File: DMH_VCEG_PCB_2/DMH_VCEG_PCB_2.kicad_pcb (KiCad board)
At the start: 2 copper layers, 96 x 175 mm, 0 parts

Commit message: Copied PCB 1 as PCB 2
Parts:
- added C1: 100pF, Capacitor_THT:C_Disc_D3.8mm_W2.6mm_P2.50mm, F.Cu at (285.9, 177.0)
- added C12: 100pF, Capacitor_THT:C_Disc_D3.8mm_W2.6mm_P2.50mm, F.Cu at (286.2, 86.7)
- added C13: 100pF, Capacitor_THT:C_Disc_D3.8mm_W2.6mm_P2.50mm, F.Cu at (286.2, 90.1)
- added C14: 100pF, Capacitor_THT:C_Disc_D3.8mm_W2.6mm_P2.50mm, F.Cu at (286.2, 93.6)
- added C15: 10nF, Capacitor_THT:C_Disc_D4.3mm_W1.9mm_P5.00mm, F.Cu at (286.2, 97.0)
- added C16: 1nF, Capacitor_THT:C_Disc_D4.3mm_W1.9mm_P5.00mm, F.Cu at (286.2, 100.5)
- added C17: 1nF, Capacitor_THT:C_Disc_D4.3mm_W1.9mm_P5.00mm, F.Cu at (286.2, 103.9)
- added C18: 1uF, Capacitor_THT:C_Disc_D4.3mm_W1.9mm_P5.00mm, F.Cu at (286.2, 107.4)
- added C19: 10uF, Capacitor_THT:CP_Radial_D5.0mm_P2.00mm, F.Cu at (242.5, 136.8)
- added C2: 100pF, Capacitor_THT:C_Disc_D3.8mm_W2.6mm_P2.50mm, F.Cu at (285.9, 180.4)
- added C20: 100nF, Capacitor_THT:C_Disc_D4.3mm_W1.9mm_P5.00mm, F.Cu at (286.2, 110.8)
- added C23: 47uF, Capacitor_THT:CP_Radial_D5.0mm_P2.00mm, B.Cu at (75.5, 46.7)
- added C24: 47uF, Capacitor_THT:CP_Radial_D5.0mm_P2.00mm, B.Cu at (124.5, 44.8)
- added C25: 100nF, Capacitor_THT:C_Disc_D4.3mm_W1.9mm_P5.00mm, F.Cu at (296.1, 157.5)
- added C26: 100nF, Capacitor_THT:C_Disc_D4.3mm_W1.9mm_P5.00mm, F.Cu at (296.1, 160.9)
- added C27: 100nF, Capacitor_THT:C_Disc_D4.3mm_W1.9mm_P5.00mm, F.Cu at (296.1, 164.4)
- added C28: 100nF, Capacitor_THT:C_Disc_D4.3mm_W1.9mm_P5.00mm, F.Cu at (296.1, 167.8)
- added C29: 100nF, Capacitor_THT:C_Disc_D4.3mm_W1.9mm_P5.00mm, F.Cu at (296.1, 171.3)
- added C3: 100pF, Capacitor_THT:C_Disc_D3.8mm_W2.6mm_P2.50mm, F.Cu at (285.9, 183.9)
- added C30: 100nF, Capacitor_THT:C_Disc_D4.3mm_W1.9mm_P5.00mm, F.Cu at (296.1, 174.7)
- added C31: 100nF, Capacitor_THT:C_Disc_D4.3mm_W1.9mm_P5.00mm, F.Cu at (296.1, 178.2)
- added C32: 100nF, Capacitor_THT:C_Disc_D4.3mm_W1.9mm_P5.00mm, F.Cu at (296.1, 181.6)
- added C33: 100nF, Capacitor_THT:C_Disc_D4.3mm_W1.9mm_P5.00mm, F.Cu at (296.1, 185.1)
- added C34: 100nF, Capacitor_THT:C_Disc_D4.3mm_W1.9mm_P5.00mm, F.Cu at (296.1, 188.5)
- added C35: 100nF, Capacitor_THT:C_Disc_D4.3mm_W1.9mm_P5.00mm, F.Cu at (304.2, 157.5)
- added C4: 10nF, Capacitor_THT:C_Disc_D4.3mm_W1.9mm_P5.00mm, F.Cu at (285.9, 187.3)
- added C40: 100nF, Capacitor_THT:C_Disc_D4.3mm_W1.9mm_P5.00mm, F.Cu at (304.2, 174.7)
- added C41: 100nF, Capacitor_THT:C_Disc_D4.3mm_W1.9mm_P5.00mm, F.Cu at (304.2, 178.2)
- added C42: 100nF, Capacitor_THT:C_Disc_D4.3mm_W1.9mm_P5.00mm, F.Cu at (304.2, 181.6)
- added C43: 100nF, Capacitor_THT:C_Disc_D4.3mm_W1.9mm_P5.00mm, F.Cu at (304.2, 185.1)
- added C44: 100nF, Capacitor_THT:C_Disc_D4.3mm_W1.9mm_P5.00mm, F.Cu at (304.2, 188.5)
- added C45: 100nF, Capacitor_THT:C_Disc_D4.3mm_W1.9mm_P5.00mm, F.Cu at (312.4, 157.5)
- added C46: 100nF, Capacitor_THT:C_Disc_D4.3mm_W1.9mm_P5.00mm, F.Cu at (312.4, 160.9)
- added C47: 100nF, Capacitor_THT:C_Disc_D4.3mm_W1.9mm_P5.00mm, F.Cu at (312.4, 164.4)
- added C48: 100nF, Capacitor_THT:C_Disc_D4.3mm_W1.9mm_P5.00mm, F.Cu at (312.4, 167.8)
- added C49: 100nF, Capacitor_THT:C_Disc_D4.3mm_W1.9mm_P5.00mm, F.Cu at (312.4, 171.3)
- added C5: 1nF, Capacitor_THT:C_Disc_D4.3mm_W1.9mm_P5.00mm, F.Cu at (285.9, 190.8)
- added C50: 100nF, Capacitor_THT:C_Disc_D4.3mm_W1.9mm_P5.00mm, F.Cu at (312.4, 174.7)
- added C6: 1nF, Capacitor_THT:C_Disc_D4.3mm_W1.9mm_P5.00mm, F.Cu at (285.9, 194.2)
- added C7: 1uF, Capacitor_THT:C_Disc_D4.3mm_W1.9mm_P5.00mm, F.Cu at (285.9, 197.7)
- added C8: 10uF, Capacitor_THT:CP_Radial_D5.0mm_P2.00mm, F.Cu at (242.2, 227.1)
- added C9: 100nF, Capacitor_THT:C_Disc_D4.3mm_W1.9mm_P5.00mm, F.Cu at (285.9, 201.1)
- added D1: SB140-, Diode_THT:D_DO-41_SOD81_P10.16mm_Horizontal, B.Cu at (117.8, 44.2)
- added D15: 1N4148, Diode_THT:D_DO-35_SOD27_P7.62mm_Horizontal, F.Cu at (282.2, 114.5)
- added D16: 1N4148, Diode_THT:D_DO-35_SOD27_P7.62mm_Horizontal, F.Cu at (282.2, 118.0)
- added D17: 1N4148, Diode_THT:D_DO-35_SOD27_P7.62mm_Horizontal, F.Cu at (282.2, 121.5)
- added D18: 1N4148, Diode_THT:D_DO-35_SOD27_P7.62mm_Horizontal, F.Cu at (282.2, 125.1)
- added D19: 1N4148, Diode_THT:D_DO-35_SOD27_P7.62mm_Horizontal, F.Cu at (282.2, 128.7)
- added D2: SB140+, Diode_THT:D_DO-41_SOD81_P10.16mm_Horizontal, B.Cu at (82.2, 54.3)
- added D20: ZPD10, Diode_THT:D_DO-35_SOD27_P7.62mm_Horizontal, F.Cu at (228.4, 135.3)
- added D3: 1N4148, Diode_THT:D_DO-35_SOD27_P7.62mm_Horizontal, F.Cu at (281.9, 204.7)
- added D4: 1N4148, Diode_THT:D_DO-35_SOD27_P7.62mm_Horizontal, F.Cu at (281.9, 208.3)
- added D5: 1N4148, Diode_THT:D_DO-35_SOD27_P7.62mm_Horizontal, F.Cu at (281.9, 211.8)
- added D6: 1N4148, Diode_THT:D_DO-35_SOD27_P7.62mm_Horizontal, F.Cu at (281.9, 215.4)
- added D7: 1N4148, Diode_THT:D_DO-35_SOD27_P7.62mm_Horizontal, F.Cu at (281.9, 218.9)
- added D8: ZPD10, Diode_THT:D_DO-35_SOD27_P7.62mm_Horizontal, F.Cu at (228.1, 225.6)
- added J1: TS_Jack_6.35mm_Sw, SynthStuff:CUI_MJ-63052A, F.Cu at (33.5, 190.2)
- added J10: TS_Jack_6.35mm_Sw, SynthStuff:CUI_MJ-63052A, F.Cu at (33.5, 208.8)
- added J100: IDC_02x08, SynthStuff:IDC-Header_2x08_P2.54mm_Vertical_Eurorack, B.Cu at (108.9, 48.8)
- added J11: TS_Jack_6.35mm_Sw, SynthStuff:CUI_MJ-63052A, F.Cu at (166.5, 190.2)
- added J12: TS_Jack_6.35mm_Sw, SynthStuff:CUI_MJ-63052A, F.Cu at (150.0, 190.2)
- added J13: TS_Jack_6.35mm_Sw, SynthStuff:CUI_MJ-63052A, F.Cu at (133.5, 190.2)
- added J14: TS_Jack_6.35mm_Sw, SynthStuff:CUI_MJ-63052A, F.Cu at (117.0, 190.2)
- added J15: TS_Jack_6.35mm_Sw, SynthStuff:CUI_MJ-63052A, F.Cu at (117.0, 208.8)
- added J16: TS_Jack_6.35mm_Sw, SynthStuff:CUI_MJ-63052A, F.Cu at (166.5, 171.8)
- added J17: TS_Jack_6.35mm_Sw, SynthStuff:CUI_MJ-63052A, F.Cu at (100.0, 208.8)
- added J18: TS_Jack_6.35mm_Sw, SynthStuff:CUI_MJ-63052A, F.Cu at (133.5, 208.8)
- added J19: TS_Jack_6.35mm_Sw, SynthStuff:CUI_MJ-63052A, F.Cu at (150.0, 208.8)
- added J2: TS_Jack_6.35mm_Sw, SynthStuff:CUI_MJ-63052A, F.Cu at (50.0, 190.2)
- added J20: TS_Jack_6.35mm_Sw, SynthStuff:CUI_MJ-63052A, F.Cu at (166.5, 208.8)
- added J200: IDC_02x08, SynthStuff:IDC-Header_2x08_P2.54mm_Vertical_BackBone, B.Cu at (91.1, 175.5)
- added J21: Conn_01x10_PinHeader, Connector_PinHeader_2.54mm:PinHeader_1x10_P2.54mm_Vertical, F.Cu at (317.1, 109.0)
- added J22: Conn_01x10_PinHeader, Connector_PinHeader_2.54mm:PinHeader_1x10_P2.54mm_Vertical, F.Cu at (321.7, 109.0)
- added J23: Conn_01x10_PinHeader, Connector_PinHeader_2.54mm:PinHeader_1x10_P2.54mm_Vertical, F.Cu at (326.2, 109.0)
- added J24: Conn_01x10_PinHeader, Connector_PinHeader_2.54mm:PinHeader_1x10_P2.54mm_Vertical, F.Cu at (301.3, 109.0)
- added J25: Conn_01x10_PinHeader, Connector_PinHeader_2.54mm:PinHeader_1x10_P2.54mm_Vertical, F.Cu at (305.9, 109.0)
- added J26: Conn_01x10_PinHeader, Connector_PinHeader_2.54mm:PinHeader_1x10_P2.54mm_Vertical, F.Cu at (310.5, 109.0)
- added J27: Conn_01x06_PinHeader, Connector_PinHeader_2.54mm:PinHeader_1x06_P2.54mm_Vertical, F.Cu at (330.8, 109.0)
- added J3: TS_Jack_6.35mm_Sw, SynthStuff:CUI_MJ-63052A, F.Cu at (66.5, 190.2)
- added J4: TS_Jack_6.35mm_Sw, SynthStuff:CUI_MJ-63052A, F.Cu at (83.0, 190.2)
- added J5: TS_Jack_6.35mm_Sw, SynthStuff:CUI_MJ-63052A, F.Cu at (83.0, 208.8)
- added J6: TS_Jack_6.35mm_Sw, SynthStuff:CUI_MJ-63052A, F.Cu at (33.5, 171.8)
- added J7: TS_Jack_6.35mm_Sw, SynthStuff:CUI_MJ-63052A, F.Cu at (100.0, 190.2)
- added J8: TS_Jack_6.35mm_Sw, SynthStuff:CUI_MJ-63052A, F.Cu at (66.5, 208.8)
- added J9: TS_Jack_6.35mm_Sw, SynthStuff:CUI_MJ-63052A, F.Cu at (50.0, 208.8)
- added Q1: BC548, Package_TO_SOT_THT:TO-92L_Inline_Wide, F.Cu at (228.0, 230.7)
- added Q2: BC558, Package_TO_SOT_THT:TO-92L_Inline_Wide, F.Cu at (241.8, 233.6)
- added Q3: BC548, Package_TO_SOT_THT:TO-92L_Inline_Wide, F.Cu at (228.0, 236.3)
- added Q5: BC548, Package_TO_SOT_THT:TO-92L_Inline_Wide, F.Cu at (228.3, 140.4)
- added Q6: BC558, Package_TO_SOT_THT:TO-92L_Inline_Wide, F.Cu at (242.1, 143.3)
- added Q7: BC548, Package_TO_SOT_THT:TO-92L_Inline_Wide, F.Cu at (228.3, 146.0)
- added R1: 100k, Resistor_THT:R_Axial_DIN0207_L6.3mm_D2.5mm_P7.62mm_Horizontal, F.Cu at (228.1, 177.3)
- added R10: 10k, Resistor_THT:R_Axial_DIN0207_L6.3mm_D2.5mm_P7.62mm_Horizontal, F.Cu at (228.1, 213.7)
- added R100: 330k, Resistor_THT:R_Axial_DIN0207_L6.3mm_D2.5mm_P7.62mm_Horizontal, F.Cu at (239.1, 119.4)
- added R101: 100k, Resistor_THT:R_Axial_DIN0207_L6.3mm_D2.5mm_P7.62mm_Horizontal, F.Cu at (239.1, 123.4)
- added R102: 680R, Resistor_THT:R_Axial_DIN0207_L6.3mm_D2.5mm_P7.62mm_Horizontal, F.Cu at (239.1, 127.5)
- added R103: 100k, Resistor_THT:R_Axial_DIN0207_L6.3mm_D2.5mm_P7.62mm_Horizontal, F.Cu at (239.1, 131.5)
- added R104: 100k, Resistor_THT:R_Axial_DIN0207_L6.3mm_D2.5mm_P7.62mm_Horizontal, F.Cu at (249.9, 87.0)
- added R105: 100k, Resistor_THT:R_Axial_DIN0207_L6.3mm_D2.5mm_P7.62mm_Horizontal, F.Cu at (249.9, 91.0)
- added R106: 470R, Resistor_THT:R_Axial_DIN0207_L6.3mm_D2.5mm_P7.62mm_Horizontal, F.Cu at (249.9, 95.1)
- added R107: 100k, Resistor_THT:R_Axial_DIN0207_L6.3mm_D2.5mm_P7.62mm_Horizontal, F.Cu at (249.9, 99.1)
- added R108: 125k, Resistor_THT:R_Axial_DIN0207_L6.3mm_D2.5mm_P7.62mm_Horizontal, F.Cu at (249.9, 103.2)
- added R109: 100k, Resistor_THT:R_Axial_DIN0207_L6.3mm_D2.5mm_P7.62mm_Horizontal, F.Cu at (249.9, 107.2)
- added R11: 10k, Resistor_THT:R_Axial_DIN0207_L6.3mm_D2.5mm_P7.62mm_Horizontal, F.Cu at (228.1, 217.8)
- added R110: 470R, Resistor_THT:R_Axial_DIN0207_L6.3mm_D2.5mm_P7.62mm_Horizontal, F.Cu at (249.9, 111.3)
- added R111: 100k, Resistor_THT:R_Axial_DIN0207_L6.3mm_D2.5mm_P7.62mm_Horizontal, F.Cu at (249.9, 115.3)
- added R112: 100k, Resistor_THT:R_Axial_DIN0207_L6.3mm_D2.5mm_P7.62mm_Horizontal, F.Cu at (249.9, 119.4)
- added R113: 10k, Resistor_THT:R_Axial_DIN0207_L6.3mm_D2.5mm_P7.62mm_Horizontal, F.Cu at (249.9, 123.4)
- added R114: 1k, Resistor_THT:R_Axial_DIN0207_L6.3mm_D2.5mm_P7.62mm_Horizontal, F.Cu at (249.9, 127.5)
- added R115: 10k, Resistor_THT:R_Axial_DIN0207_L6.3mm_D2.5mm_P7.62mm_Horizontal, F.Cu at (249.9, 131.5)
- added R116: 470k, Resistor_THT:R_Axial_DIN0207_L6.3mm_D2.5mm_P7.62mm_Horizontal, F.Cu at (260.7, 87.0)
- added R117: 10k, Resistor_THT:R_Axial_DIN0207_L6.3mm_D2.5mm_P7.62mm_Horizontal, F.Cu at (260.7, 91.0)
- added R118: 470k, Resistor_THT:R_Axial_DIN0207_L6.3mm_D2.5mm_P7.62mm_Horizontal, F.Cu at (260.7, 95.1)
- added R119: 330k, Resistor_THT:R_Axial_DIN0207_L6.3mm_D2.5mm_P7.62mm_Horizontal, F.Cu at (260.7, 99.1)
- added R12: 10k, Resistor_THT:R_Axial_DIN0207_L6.3mm_D2.5mm_P7.62mm_Horizontal, F.Cu at (228.1, 221.8)
- added R120: 10k, Resistor_THT:R_Axial_DIN0207_L6.3mm_D2.5mm_P7.62mm_Horizontal, F.Cu at (260.7, 103.2)
- added R121: 300k, Resistor_THT:R_Axial_DIN0207_L6.3mm_D2.5mm_P7.62mm_Horizontal, F.Cu at (260.7, 107.2)
- added R122: 330k, Resistor_THT:R_Axial_DIN0207_L6.3mm_D2.5mm_P7.62mm_Horizontal, F.Cu at (260.7, 111.3)
- added R123: 10k, Resistor_THT:R_Axial_DIN0207_L6.3mm_D2.5mm_P7.62mm_Horizontal, F.Cu at (260.7, 115.3)
- added R13: 470k, Resistor_THT:R_Axial_DIN0207_L6.3mm_D2.5mm_P7.62mm_Horizontal, F.Cu at (238.8, 177.3)
- added R14: 10k, Resistor_THT:R_Axial_DIN0207_L6.3mm_D2.5mm_P7.62mm_Horizontal, F.Cu at (238.8, 181.3)
- added R15: 100k, Resistor_THT:R_Axial_DIN0207_L6.3mm_D2.5mm_P7.62mm_Horizontal, F.Cu at (238.8, 185.4)
- added R16: 10k, Resistor_THT:R_Axial_DIN0207_L6.3mm_D2.5mm_P7.62mm_Horizontal, F.Cu at (238.8, 189.4)
- added R17: 10k, Resistor_THT:R_Axial_DIN0207_L6.3mm_D2.5mm_P7.62mm_Horizontal, F.Cu at (238.8, 193.5)
- added R18: 10k, Resistor_THT:R_Axial_DIN0207_L6.3mm_D2.5mm_P7.62mm_Horizontal, F.Cu at (238.8, 197.5)
- added R19: 100k, Resistor_THT:R_Axial_DIN0207_L6.3mm_D2.5mm_P7.62mm_Horizontal, F.Cu at (238.8, 201.6)
- added R2: 100k, Resistor_THT:R_Axial_DIN0207_L6.3mm_D2.5mm_P7.62mm_Horizontal, F.Cu at (228.1, 181.3)
- added R20: 300k, Resistor_THT:R_Axial_DIN0207_L6.3mm_D2.5mm_P7.62mm_Horizontal, F.Cu at (238.8, 205.6)
- added R21: 330k, Resistor_THT:R_Axial_DIN0207_L6.3mm_D2.5mm_P7.62mm_Horizontal, F.Cu at (238.8, 209.7)
- added R22: 100k, Resistor_THT:R_Axial_DIN0207_L6.3mm_D2.5mm_P7.62mm_Horizontal, F.Cu at (238.8, 213.7)
- added R23: 680R, Resistor_THT:R_Axial_DIN0207_L6.3mm_D2.5mm_P7.62mm_Horizontal, F.Cu at (238.8, 217.8)
- added R24: 100k, Resistor_THT:R_Axial_DIN0207_L6.3mm_D2.5mm_P7.62mm_Horizontal, F.Cu at (238.8, 221.8)
- added R25: 100k, Resistor_THT:R_Axial_DIN0207_L6.3mm_D2.5mm_P7.62mm_Horizontal, F.Cu at (249.6, 177.3)
- added R26: 100k, Resistor_THT:R_Axial_DIN0207_L6.3mm_D2.5mm_P7.62mm_Horizontal, F.Cu at (249.6, 181.3)
- added R27: 470R, Resistor_THT:R_Axial_DIN0207_L6.3mm_D2.5mm_P7.62mm_Horizontal, F.Cu at (249.6, 185.4)
- added R28: 100k, Resistor_THT:R_Axial_DIN0207_L6.3mm_D2.5mm_P7.62mm_Horizontal, F.Cu at (249.6, 189.4)
- added R29: 125k, Resistor_THT:R_Axial_DIN0207_L6.3mm_D2.5mm_P7.62mm_Horizontal, F.Cu at (249.6, 193.5)
- added R3: 22k, Resistor_THT:R_Axial_DIN0207_L6.3mm_D2.5mm_P7.62mm_Horizontal, F.Cu at (228.1, 185.4)
- added R30: 100k, Resistor_THT:R_Axial_DIN0207_L6.3mm_D2.5mm_P7.62mm_Horizontal, F.Cu at (249.6, 197.5)
- added R31: 470R, Resistor_THT:R_Axial_DIN0207_L6.3mm_D2.5mm_P7.62mm_Horizontal, F.Cu at (249.6, 201.6)
- added R32: 100k, Resistor_THT:R_Axial_DIN0207_L6.3mm_D2.5mm_P7.62mm_Horizontal, F.Cu at (249.6, 205.6)
- added R33: 100k, Resistor_THT:R_Axial_DIN0207_L6.3mm_D2.5mm_P7.62mm_Horizontal, F.Cu at (249.6, 209.7)
- added R34: 10k, Resistor_THT:R_Axial_DIN0207_L6.3mm_D2.5mm_P7.62mm_Horizontal, F.Cu at (249.6, 213.7)
- added R35: 1k, Resistor_THT:R_Axial_DIN0207_L6.3mm_D2.5mm_P7.62mm_Horizontal, F.Cu at (249.6, 217.8)
- added R36: 10k, Resistor_THT:R_Axial_DIN0207_L6.3mm_D2.5mm_P7.62mm_Horizontal, F.Cu at (249.6, 221.8)
- added R37: 470k, Resistor_THT:R_Axial_DIN0207_L6.3mm_D2.5mm_P7.62mm_Horizontal, F.Cu at (260.4, 177.3)
- added R38: 10k, Resistor_THT:R_Axial_DIN0207_L6.3mm_D2.5mm_P7.62mm_Horizontal, F.Cu at (260.4, 181.3)
- added R39: 470k, Resistor_THT:R_Axial_DIN0207_L6.3mm_D2.5mm_P7.62mm_Horizontal, F.Cu at (260.4, 185.4)
- added R4: 100k, Resistor_THT:R_Axial_DIN0207_L6.3mm_D2.5mm_P7.62mm_Horizontal, F.Cu at (228.1, 189.4)
- added R40: 330k, Resistor_THT:R_Axial_DIN0207_L6.3mm_D2.5mm_P7.62mm_Horizontal, F.Cu at (260.4, 189.4)
- added R41: 10k, Resistor_THT:R_Axial_DIN0207_L6.3mm_D2.5mm_P7.62mm_Horizontal, F.Cu at (260.4, 193.5)
- added R42: 300k, Resistor_THT:R_Axial_DIN0207_L6.3mm_D2.5mm_P7.62mm_Horizontal, F.Cu at (260.4, 197.5)
- added R43: 330k, Resistor_THT:R_Axial_DIN0207_L6.3mm_D2.5mm_P7.62mm_Horizontal, F.Cu at (260.4, 201.6)
- added R44: 10k, Resistor_THT:R_Axial_DIN0207_L6.3mm_D2.5mm_P7.62mm_Horizontal, F.Cu at (260.4, 205.6)
- added R5: 22k, Resistor_THT:R_Axial_DIN0207_L6.3mm_D2.5mm_P7.62mm_Horizontal, F.Cu at (228.1, 193.5)
- added R6: 1M, Resistor_THT:R_Axial_DIN0207_L6.3mm_D2.5mm_P7.62mm_Horizontal, F.Cu at (228.1, 197.5)
- added R7: 1M, Resistor_THT:R_Axial_DIN0207_L6.3mm_D2.5mm_P7.62mm_Horizontal, F.Cu at (228.1, 201.6)
- added R8: 22k, Resistor_THT:R_Axial_DIN0207_L6.3mm_D2.5mm_P7.62mm_Horizontal, F.Cu at (228.1, 205.6)
- added R80: 100k, Resistor_THT:R_Axial_DIN0207_L6.3mm_D2.5mm_P7.62mm_Horizontal, F.Cu at (228.4, 87.0)
- added R81: 100k, Resistor_THT:R_Axial_DIN0207_L6.3mm_D2.5mm_P7.62mm_Horizontal, F.Cu at (228.4, 91.0)
- added R82: 22k, Resistor_THT:R_Axial_DIN0207_L6.3mm_D2.5mm_P7.62mm_Horizontal, F.Cu at (228.4, 95.1)
- added R83: 100k, Resistor_THT:R_Axial_DIN0207_L6.3mm_D2.5mm_P7.62mm_Horizontal, F.Cu at (228.4, 99.1)
- added R84: 22k, Resistor_THT:R_Axial_DIN0207_L6.3mm_D2.5mm_P7.62mm_Horizontal, F.Cu at (228.4, 103.2)
- added R85: 1M, Resistor_THT:R_Axial_DIN0207_L6.3mm_D2.5mm_P7.62mm_Horizontal, F.Cu at (228.4, 107.2)
- added R86: 1M, Resistor_THT:R_Axial_DIN0207_L6.3mm_D2.5mm_P7.62mm_Horizontal, F.Cu at (228.4, 111.3)
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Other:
- board size 96 x 175 mm -> 148 x 175 mm

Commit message: Placed front panel components on PCB 2
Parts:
- removed C1, C12, C13, C14, C2, C3: 100pF, Capacitor_THT:C_Disc_D3.8mm_W2.6mm_P2.50mm
- removed C15, C4: 10nF, Capacitor_THT:C_Disc_D4.3mm_W1.9mm_P5.00mm
- removed C16, C17, C5, C6: 1nF, Capacitor_THT:C_Disc_D4.3mm_W1.9mm_P5.00mm
- removed C18, C7: 1uF, Capacitor_THT:C_Disc_D4.3mm_W1.9mm_P5.00mm
- removed C19, C8: 10uF, Capacitor_THT:CP_Radial_D5.0mm_P2.00mm
- removed C20, C25, C26, C27, C28, C29, C30, C31, C32, C33, C34, C35, C40, C41, C42, C43, C44, C45, C46, C47, C48, C49, C50, C9: 100nF, Capacitor_THT:C_Disc_D4.3mm_W1.9mm_P5.00mm
- removed C23, C24: 47uF, Capacitor_THT:CP_Radial_D5.0mm_P2.00mm
- removed D1: SB140-, Diode_THT:D_DO-41_SOD81_P10.16mm_Horizontal
- removed D15, D16, D17, D18, D19, D3, D4, D5, D6, D7: 1N4148, Diode_THT:D_DO-35_SOD27_P7.62mm_Horizontal
- removed D2: SB140+, Diode_THT:D_DO-41_SOD81_P10.16mm_Horizontal
- removed D20, D8: ZPD10, Diode_THT:D_DO-35_SOD27_P7.62mm_Horizontal
- removed J1, J10, J11, J12, J13, J14, J15, J16, J17, J18, J19, J2, J20, J3, J4, J5, J6, J7, J8, J9: TS_Jack_6.35mm_Sw, SynthStuff:CUI_MJ-63052A
- removed J100: IDC_02x08, SynthStuff:IDC-Header_2x08_P2.54mm_Vertical_Eurorack
- removed J200: IDC_02x08, SynthStuff:IDC-Header_2x08_P2.54mm_Vertical_BackBone
- removed Q1, Q3, Q5, Q7: BC548, Package_TO_SOT_THT:TO-92L_Inline_Wide
- removed Q2, Q6: BC558, Package_TO_SOT_THT:TO-92L_Inline_Wide
- removed R1, R101, R103, R104, R105, R107, R109, R111, R112, R15, R19, R2, R22, R24, R25, R26, R28, R30, R32, R33, R4, R80, R81, R83, R94, R98: 100k, Resistor_THT:R_Axial_DIN0207_L6.3mm_D2.5mm_P7.62mm_Horizontal
- removed R10, R11, R113, R115, R117, R12, R120, R123, R14, R16, R17, R18, R34, R36, R38, R41, R44, R89, R90, R91, R93, R95, R96, R97: 10k, Resistor_THT:R_Axial_DIN0207_L6.3mm_D2.5mm_P7.62mm_Horizontal
- removed R100, R119, R122, R21, R40, R43: 330k, Resistor_THT:R_Axial_DIN0207_L6.3mm_D2.5mm_P7.62mm_Horizontal
- removed R102, R23: 680R, Resistor_THT:R_Axial_DIN0207_L6.3mm_D2.5mm_P7.62mm_Horizontal
- removed R106, R110, R27, R31, R88, R9: 470R, Resistor_THT:R_Axial_DIN0207_L6.3mm_D2.5mm_P7.62mm_Horizontal
- removed R108, R29: 125k, Resistor_THT:R_Axial_DIN0207_L6.3mm_D2.5mm_P7.62mm_Horizontal
- removed R114, R35: 1k, Resistor_THT:R_Axial_DIN0207_L6.3mm_D2.5mm_P7.62mm_Horizontal
- removed R116, R118, R13, R37, R39, R92: 470k, Resistor_THT:R_Axial_DIN0207_L6.3mm_D2.5mm_P7.62mm_Horizontal
- removed R121, R20, R42, R99: 300k, Resistor_THT:R_Axial_DIN0207_L6.3mm_D2.5mm_P7.62mm_Horizontal
- removed R3, R5, R8, R82, R84, R87: 22k, Resistor_THT:R_Axial_DIN0207_L6.3mm_D2.5mm_P7.62mm_Horizontal
- removed R6, R7, R85, R86: 1M, Resistor_THT:R_Axial_DIN0207_L6.3mm_D2.5mm_P7.62mm_Horizontal
- removed RV1, RV12, RV2, RV31, RV32, RV36, RV37, RV38, RV42, RV6, RV7, RV8: 50k, Potentiometer_THT:Potentiometer_Bourns_3296W_Vertical
- removed RV11, RV41: 10k, Potentiometer_THT:Potentiometer_Bourns_3296W_Vertical
- removed RV13, RV3, RV33, RV39, RV43, RV9: 100k, Potentiometer_THT:Potentiometer_Bourns_3296W_Vertical
- removed U11, U2: 4001, Package_DIP:DIP-14_W7.62mm_Socket
- removed U12, U3: 40106, Package_DIP:DIP-14_W7.62mm_Socket
- removed U13, U4: CD4066BE, Package_DIP:DIP-14_W7.62mm
- removed U14, U15, U16, U5, U6, U7: TL074, Package_DIP:DIP-14_W7.62mm_Socket
- added C10: 1uF, Capacitor_THT:C_Disc_D4.3mm_W1.9mm_P5.00mm, F.Cu at (214.2, 123.2)
- added C11: 10uF, Capacitor_THT:CP_Radial_D5.0mm_P2.00mm, F.Cu at (231.3, 124.8)
- added C21: 1uF, Capacitor_THT:C_Disc_D4.3mm_W1.9mm_P5.00mm, F.Cu at (261.0, 155.1)
- added C22: 10uF, Capacitor_THT:CP_Radial_D5.0mm_P2.00mm, F.Cu at (223.1, 173.6)
- added C36: 100nF, Capacitor_THT:C_Disc_D4.3mm_W1.9mm_P5.00mm, F.Cu at (333.2, 86.8)
- added C37: 100nF, Capacitor_THT:C_Disc_D4.3mm_W1.9mm_P5.00mm, F.Cu at (333.2, 90.2)
- added C38: 100nF, Capacitor_THT:C_Disc_D4.3mm_W1.9mm_P5.00mm, F.Cu at (333.2, 93.7)
- added C39: 100nF, Capacitor_THT:C_Disc_D4.3mm_W1.9mm_P5.00mm, F.Cu at (333.2, 97.2)
- added C51: 100nF, Capacitor_THT:C_Disc_D4.3mm_W1.9mm_P5.00mm, F.Cu at (333.2, 100.6)
- added C52: 100nF, Capacitor_THT:C_Disc_D4.3mm_W1.9mm_P5.00mm, F.Cu at (333.2, 104.0)
- added C53: 100nF, Capacitor_THT:C_Disc_D4.3mm_W1.9mm_P5.00mm, F.Cu at (333.2, 107.5)
- added C54: 100nF, Capacitor_THT:C_Disc_D4.3mm_W1.9mm_P5.00mm, F.Cu at (333.2, 111.0)
- added C55: 1nF, Capacitor_THT:C_Disc_D4.3mm_W1.9mm_P5.00mm, F.Cu at (214.2, 126.7)
- added C56: 1nF, Capacitor_THT:C_Disc_D4.3mm_W1.9mm_P5.00mm, F.Cu at (261.0, 158.5)
- added C57: 100nF, Capacitor_THT:C_Disc_D4.3mm_W1.9mm_P5.00mm, F.Cu at (333.2, 114.4)
- added C58: 100nF, Capacitor_THT:C_Disc_D4.3mm_W1.9mm_P5.00mm, F.Cu at (333.2, 117.8)
- added C59: 1nF, Capacitor_THT:C_Disc_D4.3mm_W1.9mm_P5.00mm, F.Cu at (214.2, 130.2)
- added C60: 1nF, Capacitor_THT:C_Disc_D4.3mm_W1.9mm_P5.00mm, F.Cu at (261.0, 162.0)
- added C61: 100nF, Capacitor_THT:C_Disc_D4.3mm_W1.9mm_P5.00mm, F.Cu at (333.2, 121.3)
- added C62: 100nF, Capacitor_THT:C_Disc_D4.3mm_W1.9mm_P5.00mm, F.Cu at (333.2, 124.8)
- added D10: 1N4148, Diode_THT:D_DO-35_SOD27_P7.62mm_Horizontal, F.Cu at (252.4, 124.5)
- added D11: LED_Red, LED_THT:LED_D3.0mm, F.Cu at (68.7, 54.8)
- added D12: LED_Red, LED_THT:LED_D3.0mm, F.Cu at (68.7, 85.8)
- added D13: LED_Red, LED_THT:LED_D3.0mm, F.Cu at (68.7, 116.8)
- added D14: LED_Red, LED_THT:LED_D3.0mm, F.Cu at (68.7, 147.8)
- added D21: 1N4148, Diode_THT:D_DO-35_SOD27_P7.62mm_Horizontal, F.Cu at (252.4, 169.8)
- added D22: 1N4148, Diode_THT:D_DO-35_SOD27_P7.62mm_Horizontal, F.Cu at (252.4, 173.3)
- added D23: LED_Red, LED_THT:LED_D3.0mm, F.Cu at (128.5, 54.8)
- added D24: LED_Red, LED_THT:LED_D3.0mm, F.Cu at (128.5, 85.8)
- added D25: LED_Red, LED_THT:LED_D3.0mm, F.Cu at (128.5, 116.8)
- added D26: LED_Red, LED_THT:LED_D3.0mm, F.Cu at (128.5, 147.8)
- added D27: 1N4148, Diode_THT:D_DO-35_SOD27_P7.62mm_Horizontal, F.Cu at (252.4, 128.1)
- added D28: 1N4148, Diode_THT:D_DO-35_SOD27_P7.62mm_Horizontal, F.Cu at (252.4, 176.9)
- added D9: 1N4148, Diode_THT:D_DO-35_SOD27_P7.62mm_Horizontal, F.Cu at (252.4, 121.0)
- added J0: Conn_01x01, Connector_PinHeader_2.54mm:PinHeader_1x01_P2.54mm_Vertical, F.Cu at (30.0, 127.2)
- added Q4: BC548, Package_TO_SOT_THT:TO-92L_Inline_Wide, F.Cu at (222.3, 124.8)
- added Q8: BC548, Package_TO_SOT_THT:TO-92L_Inline_Wide, F.Cu at (214.1, 173.6)
- added R124: 100k, Resistor_THT:R_Axial_DIN0207_L6.3mm_D2.5mm_P7.62mm_Horizontal, F.Cu at (214.2, 139.9)
- added R125: 100k, Resistor_THT:R_Axial_DIN0207_L6.3mm_D2.5mm_P7.62mm_Horizontal, F.Cu at (214.2, 144.0)
- added R126: 100k, Resistor_THT:R_Axial_DIN0207_L6.3mm_D2.5mm_P7.62mm_Horizontal, F.Cu at (214.2, 148.1)
- added R127: 47k, Resistor_THT:R_Axial_DIN0207_L6.3mm_D2.5mm_P7.62mm_Horizontal, F.Cu at (214.2, 152.1)
- added R128: 470R, Resistor_THT:R_Axial_DIN0207_L6.3mm_D2.5mm_P7.62mm_Horizontal, F.Cu at (214.2, 156.2)
- added R129: 100R, Resistor_THT:R_Axial_DIN0207_L6.3mm_D2.5mm_P7.62mm_Horizontal, F.Cu at (214.2, 160.2)
- added R130: 10k, Resistor_THT:R_Axial_DIN0207_L6.3mm_D2.5mm_P7.62mm_Horizontal, F.Cu at (214.2, 164.2)
- added R131: 680R, Resistor_THT:R_Axial_DIN0207_L6.3mm_D2.5mm_P7.62mm_Horizontal, F.Cu at (214.2, 168.3)
- added R132: 100k, Resistor_THT:R_Axial_DIN0207_L6.3mm_D2.5mm_P7.62mm_Horizontal, F.Cu at (224.9, 135.9)
- added R133: 100k, Resistor_THT:R_Axial_DIN0207_L6.3mm_D2.5mm_P7.62mm_Horizontal, F.Cu at (224.9, 139.9)
- added R134: 100k, Resistor_THT:R_Axial_DIN0207_L6.3mm_D2.5mm_P7.62mm_Horizontal, F.Cu at (224.9, 144.0)
- added R135: 68K, Resistor_THT:R_Axial_DIN0207_L6.3mm_D2.5mm_P7.62mm_Horizontal, F.Cu at (224.9, 148.1)
- added R136: 2k2, Resistor_THT:R_Axial_DIN0207_L6.3mm_D2.5mm_P7.62mm_Horizontal, F.Cu at (224.9, 152.1)
- added R137: 2k2, Resistor_THT:R_Axial_DIN0207_L6.3mm_D2.5mm_P7.62mm_Horizontal, F.Cu at (224.9, 156.2)
- added R138: 2k2, Resistor_THT:R_Axial_DIN0207_L6.3mm_D2.5mm_P7.62mm_Horizontal, F.Cu at (224.9, 160.2)
- added R139: 2k2, Resistor_THT:R_Axial_DIN0207_L6.3mm_D2.5mm_P7.62mm_Horizontal, F.Cu at (224.9, 164.2)
- added R140: 68K, Resistor_THT:R_Axial_DIN0207_L6.3mm_D2.5mm_P7.62mm_Horizontal, F.Cu at (224.9, 168.3)
- added R141: 100k, Resistor_THT:R_Axial_DIN0207_L6.3mm_D2.5mm_P7.62mm_Horizontal, F.Cu at (235.7, 135.9)
- added R142: 1k, Resistor_THT:R_Axial_DIN0207_L6.3mm_D2.5mm_P7.62mm_Horizontal, F.Cu at (235.7, 139.9)
- added R143: 100k, Resistor_THT:R_Axial_DIN0207_L6.3mm_D2.5mm_P7.62mm_Horizontal, F.Cu at (235.7, 144.0)
- added R144: 1k, Resistor_THT:R_Axial_DIN0207_L6.3mm_D2.5mm_P7.62mm_Horizontal, F.Cu at (235.7, 148.1)
- added R145: 100k, Resistor_THT:R_Axial_DIN0207_L6.3mm_D2.5mm_P7.62mm_Horizontal, F.Cu at (285.2, 77.0)
- added R146: 100k, Resistor_THT:R_Axial_DIN0207_L6.3mm_D2.5mm_P7.62mm_Horizontal, F.Cu at (285.2, 81.0)
- added R147: 100k, Resistor_THT:R_Axial_DIN0207_L6.3mm_D2.5mm_P7.62mm_Horizontal, F.Cu at (214.2, 77.0)
- added R148: 100k, Resistor_THT:R_Axial_DIN0207_L6.3mm_D2.5mm_P7.62mm_Horizontal, F.Cu at (214.2, 81.0)
- added R149: 10k, Resistor_THT:R_Axial_DIN0207_L6.3mm_D2.5mm_P7.62mm_Horizontal, F.Cu at (235.7, 95.2)
- added R150: 100k, Resistor_THT:R_Axial_DIN0207_L6.3mm_D2.5mm_P7.62mm_Horizontal, F.Cu at (235.7, 99.2)
- added R151: 100k, Resistor_THT:R_Axial_DIN0207_L6.3mm_D2.5mm_P7.62mm_Horizontal, F.Cu at (235.7, 103.3)
- added R152: 100k, Resistor_THT:R_Axial_DIN0207_L6.3mm_D2.5mm_P7.62mm_Horizontal, F.Cu at (235.7, 107.3)
- added R153: 100k, Resistor_THT:R_Axial_DIN0207_L6.3mm_D2.5mm_P7.62mm_Horizontal, F.Cu at (235.7, 111.4)
- added R154: 10k, Resistor_THT:R_Axial_DIN0207_L6.3mm_D2.5mm_P7.62mm_Horizontal, F.Cu at (235.7, 115.5)
- added R155: 100k, Resistor_THT:R_Axial_DIN0207_L6.3mm_D2.5mm_P7.62mm_Horizontal, F.Cu at (235.7, 152.1)
- added R156: 100k, Resistor_THT:R_Axial_DIN0207_L6.3mm_D2.5mm_P7.62mm_Horizontal, F.Cu at (235.7, 156.2)
- added R157: 100k, Resistor_THT:R_Axial_DIN0207_L6.3mm_D2.5mm_P7.62mm_Horizontal, F.Cu at (235.7, 160.2)
- added R158: 10k, Resistor_THT:R_Axial_DIN0207_L6.3mm_D2.5mm_P7.62mm_Horizontal, F.Cu at (235.7, 164.2)
- added R45: 100k, Resistor_THT:R_Axial_DIN0207_L6.3mm_D2.5mm_P7.62mm_Horizontal, F.Cu at (214.2, 87.1)
- added R46: 100k, Resistor_THT:R_Axial_DIN0207_L6.3mm_D2.5mm_P7.62mm_Horizontal, F.Cu at (214.2, 91.2)
- added R47: 100k, Resistor_THT:R_Axial_DIN0207_L6.3mm_D2.5mm_P7.62mm_Horizontal, F.Cu at (214.2, 95.2)
- added R48: 100k, Resistor_THT:R_Axial_DIN0207_L6.3mm_D2.5mm_P7.62mm_Horizontal, F.Cu at (214.2, 99.2)
- added R49: 470R, Resistor_THT:R_Axial_DIN0207_L6.3mm_D2.5mm_P7.62mm_Horizontal, F.Cu at (214.2, 103.3)
- added R50: 47k, Resistor_THT:R_Axial_DIN0207_L6.3mm_D2.5mm_P7.62mm_Horizontal, F.Cu at (214.2, 107.3)
- added R51: 100R, Resistor_THT:R_Axial_DIN0207_L6.3mm_D2.5mm_P7.62mm_Horizontal, F.Cu at (214.2, 111.4)
- added R52: 680R, Resistor_THT:R_Axial_DIN0207_L6.3mm_D2.5mm_P7.62mm_Horizontal, F.Cu at (214.2, 115.5)
- added R53: 100k, Resistor_THT:R_Axial_DIN0207_L6.3mm_D2.5mm_P7.62mm_Horizontal, F.Cu at (214.2, 119.5)
- added R54: 100k, Resistor_THT:R_Axial_DIN0207_L6.3mm_D2.5mm_P7.62mm_Horizontal, F.Cu at (214.2, 135.9)
- added R55: 100k, Resistor_THT:R_Axial_DIN0207_L6.3mm_D2.5mm_P7.62mm_Horizontal, F.Cu at (224.9, 87.1)
- added R56: 68K, Resistor_THT:R_Axial_DIN0207_L6.3mm_D2.5mm_P7.62mm_Horizontal, F.Cu at (224.9, 91.2)
- added R57: 2k2, Resistor_THT:R_Axial_DIN0207_L6.3mm_D2.5mm_P7.62mm_Horizontal, F.Cu at (224.9, 95.2)
- added R58: 2k2, Resistor_THT:R_Axial_DIN0207_L6.3mm_D2.5mm_P7.62mm_Horizontal, F.Cu at (224.9, 99.2)
- added R59: 2k2, Resistor_THT:R_Axial_DIN0207_L6.3mm_D2.5mm_P7.62mm_Horizontal, F.Cu at (224.9, 103.3)
- added R60: 2k2, Resistor_THT:R_Axial_DIN0207_L6.3mm_D2.5mm_P7.62mm_Horizontal, F.Cu at (224.9, 107.3)
- added R61: 68K, Resistor_THT:R_Axial_DIN0207_L6.3mm_D2.5mm_P7.62mm_Horizontal, F.Cu at (224.9, 111.4)
- added R62: 100k, Resistor_THT:R_Axial_DIN0207_L6.3mm_D2.5mm_P7.62mm_Horizontal, F.Cu at (224.9, 115.5)
- added R63: 1k, Resistor_THT:R_Axial_DIN0207_L6.3mm_D2.5mm_P7.62mm_Horizontal, F.Cu at (224.9, 119.5)
- added R64: 100k, Resistor_THT:R_Axial_DIN0207_L6.3mm_D2.5mm_P7.62mm_Horizontal, F.Cu at (235.7, 87.1)
- added R65: 1k, Resistor_THT:R_Axial_DIN0207_L6.3mm_D2.5mm_P7.62mm_Horizontal, F.Cu at (235.7, 91.2)
- added R66: 33k, Resistor_THT:R_Axial_DIN0207_L6.3mm_D2.5mm_P7.62mm_Horizontal, F.Cu at (285.2, 48.6)
- added R67: 33k, Resistor_THT:R_Axial_DIN0207_L6.3mm_D2.5mm_P7.62mm_Horizontal, F.Cu at (285.2, 52.7)
- added R68: 33k, Resistor_THT:R_Axial_DIN0207_L6.3mm_D2.5mm_P7.62mm_Horizontal, F.Cu at (285.2, 56.8)
- added R69: 33k, Resistor_THT:R_Axial_DIN0207_L6.3mm_D2.5mm_P7.62mm_Horizontal, F.Cu at (285.2, 60.8)
- added R70: 1k, Resistor_THT:R_Axial_DIN0207_L6.3mm_D2.5mm_P7.62mm_Horizontal, F.Cu at (285.2, 64.8)
- added R71: 100k, Resistor_THT:R_Axial_DIN0207_L6.3mm_D2.5mm_P7.62mm_Horizontal, F.Cu at (285.2, 68.9)
- added R72: 100k, Resistor_THT:R_Axial_DIN0207_L6.3mm_D2.5mm_P7.62mm_Horizontal, F.Cu at (285.2, 73.0)
- added R73: 33k, Resistor_THT:R_Axial_DIN0207_L6.3mm_D2.5mm_P7.62mm_Horizontal, F.Cu at (214.2, 48.6)
- added R74: 33k, Resistor_THT:R_Axial_DIN0207_L6.3mm_D2.5mm_P7.62mm_Horizontal, F.Cu at (214.2, 52.7)
- added R75: 33k, Resistor_THT:R_Axial_DIN0207_L6.3mm_D2.5mm_P7.62mm_Horizontal, F.Cu at (214.2, 56.8)
- added R76: 33k, Resistor_THT:R_Axial_DIN0207_L6.3mm_D2.5mm_P7.62mm_Horizontal, F.Cu at (214.2, 60.8)
- added R77: 1k, Resistor_THT:R_Axial_DIN0207_L6.3mm_D2.5mm_P7.62mm_Horizontal, F.Cu at (214.2, 64.8)
- added R78: 100k, Resistor_THT:R_Axial_DIN0207_L6.3mm_D2.5mm_P7.62mm_Horizontal, F.Cu at (214.2, 68.9)
- added R79: 100k, Resistor_THT:R_Axial_DIN0207_L6.3mm_D2.5mm_P7.62mm_Horizontal, F.Cu at (214.2, 73.0)
- added RV10: 100k, SynthStuff:Potentiometer_Alpha_RD901F-40-00D_Single_Vertical, F.Cu at (47.5, 62.2)
- added RV14: 100k, SynthStuff:Potentiometer_Alpha_RD901F-40-00D_Single_Vertical, F.Cu at (47.5, 162.2)
- added RV15: 100k, SynthStuff:Potentiometer_TT_P110KH1, F.Cu at (85.0, 65.8)
- added RV16: 100k, SynthStuff:Potentiometer_TT_P110KH1, F.Cu at (85.0, 94.2)
- added RV17: 100k, SynthStuff:Potentiometer_TT_P110KH1, F.Cu at (85.0, 122.8)
- added RV18: 100k, SynthStuff:Potentiometer_TT_P110KH1, F.Cu at (85.0, 151.2)
- added RV19: 50k, Potentiometer_THT:Potentiometer_Bourns_3296X_Horizontal, F.Cu at (304.0, 49.8)
- added RV20: 50k, Potentiometer_THT:Potentiometer_Bourns_3296X_Horizontal, F.Cu at (304.0, 56.2)
- added RV21: 50k, Potentiometer_THT:Potentiometer_Bourns_3296X_Horizontal, F.Cu at (304.0, 62.6)
- added RV22: 50k, Potentiometer_THT:Potentiometer_Bourns_3296X_Horizontal, F.Cu at (304.0, 69.0)
- added RV23: 100k, SynthStuff:Potentiometer_TT_P110KH1, F.Cu at (110.0, 65.8)
- added RV24: 100k, SynthStuff:Potentiometer_TT_P110KH1, F.Cu at (110.0, 94.2)
- added RV25: 100k, SynthStuff:Potentiometer_TT_P110KH1, F.Cu at (110.0, 122.8)
- added RV26: 100k, SynthStuff:Potentiometer_TT_P110KH1, F.Cu at (110.0, 151.2)
- added RV27: 50k, Potentiometer_THT:Potentiometer_Bourns_3296X_Horizontal, F.Cu at (233.0, 49.8)
- added RV28: 50k, Potentiometer_THT:Potentiometer_Bourns_3296X_Horizontal, F.Cu at (233.0, 56.2)
- added RV29: 50k, Potentiometer_THT:Potentiometer_Bourns_3296X_Horizontal, F.Cu at (233.0, 62.6)
- added RV30: 50k, Potentiometer_THT:Potentiometer_Bourns_3296X_Horizontal, F.Cu at (233.0, 69.0)
- added RV34: 100k, SynthStuff:Potentiometer_Alpha_RD901F-40-00D_Single_Vertical, F.Cu at (147.5, 95.8)
- added RV35: 100k, SynthStuff:Potentiometer_Alpha_RD901F-40-00D_Single_Vertical, F.Cu at (147.5, 129.2)
- added RV4: 100k, SynthStuff:Potentiometer_Alpha_RD901F-40-00D_Single_Vertical, F.Cu at (47.5, 95.8)
- added RV40: 100k, SynthStuff:Potentiometer_Alpha_RD901F-40-00D_Single_Vertical, F.Cu at (147.5, 62.2)
- added RV44: 100k, SynthStuff:Potentiometer_Alpha_RD901F-40-00D_Single_Vertical, F.Cu at (147.5, 162.2)
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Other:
- board size 148 x 175 mm -> 148 x 139 mm

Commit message: Placed ICs and pin headers on PCB 2
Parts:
- removed J0: Conn_01x01, Connector_PinHeader_2.54mm:PinHeader_1x01_P2.54mm_Vertical
- removed U1, U10: TL074, Package_DIP:DIP-14_W7.62mm_Socket
- J21, J22, J23, J24, J25, J26: footprint Connector_PinHeader_2.54mm:PinHeader_1x10_P2.54mm_Vertical -> Connector_PinSocket_2.54mm:PinSocket_1x10_P2.54mm_Vertical; moved to B.Cu
- J27: footprint Connector_PinHeader_2.54mm:PinHeader_1x06_P2.54mm_Vertical -> Connector_PinSocket_2.54mm:PinSocket_1x06_P2.54mm_Vertical; moved to B.Cu
- U21: footprint Package_DIP:DIP-8_W7.62mm -> Package_DIP:DIP-8_W7.62mm_Socket
- moved RV22 275.0 mm to (35.8, 130.0)
- moved RV21 274.5 mm to (35.8, 121.0)
- moved RV20 269.6 mm to (35.8, 84.0)
- moved RV19 269.4 mm to (35.8, 75.0)
- moved U9 245.4 mm to (64.0, 62.0)
- moved U21 220.6 mm to (96.2, 128.0)
- moved U19 198.2 mm to (64.0, 124.5)
- moved U8 183.1 mm to (64.0, 93.5)
- moved J23 179.9 mm to (28.2, 137.8), turned to 180 degrees
- moved Q4 177.7 mm to (45.5, 143.0), turned to -90 degrees
- moved J21 171.9 mm to (28.2, 45.8), turned to 180 degrees
- moved J22 169.8 mm to (28.2, 91.8), turned to 180 degrees
- moved U20 131.2 mm to (128.0, 124.5)
- moved J27 129.7 mm to (93.7, 156.0), turned to -90 degrees
- moved U17 126.3 mm to (128.0, 93.5)
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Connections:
- C10 pad 1: Net-(C10-Pad1) -> Net-(J23D-Pin_4)
- C11 pad 1: Net-(C10-Pad1) -> Net-(J23D-Pin_4)
- C21 pad 1: Net-(C21-Pad1) -> Net-(J26D-Pin_4)
- C22 pad 1: Net-(C21-Pad1) -> Net-(J26D-Pin_4)
- J23 pad 4: /Core Circuit A/Proc Gate -> Net-(J23D-Pin_4)
- J26 pad 4: /Core Circuit B/Proc Gate -> Net-(J26D-Pin_4)
- R131 pad 1: Net-(C21-Pad1) -> Net-(J26D-Pin_4)
- R132 pad 1: Net-(C21-Pad1) -> Net-(J26D-Pin_4)
- R52 pad 1: Net-(C10-Pad1) -> Net-(J23D-Pin_4)
- R53 pad 1: Net-(C10-Pad1) -> Net-(J23D-Pin_4)

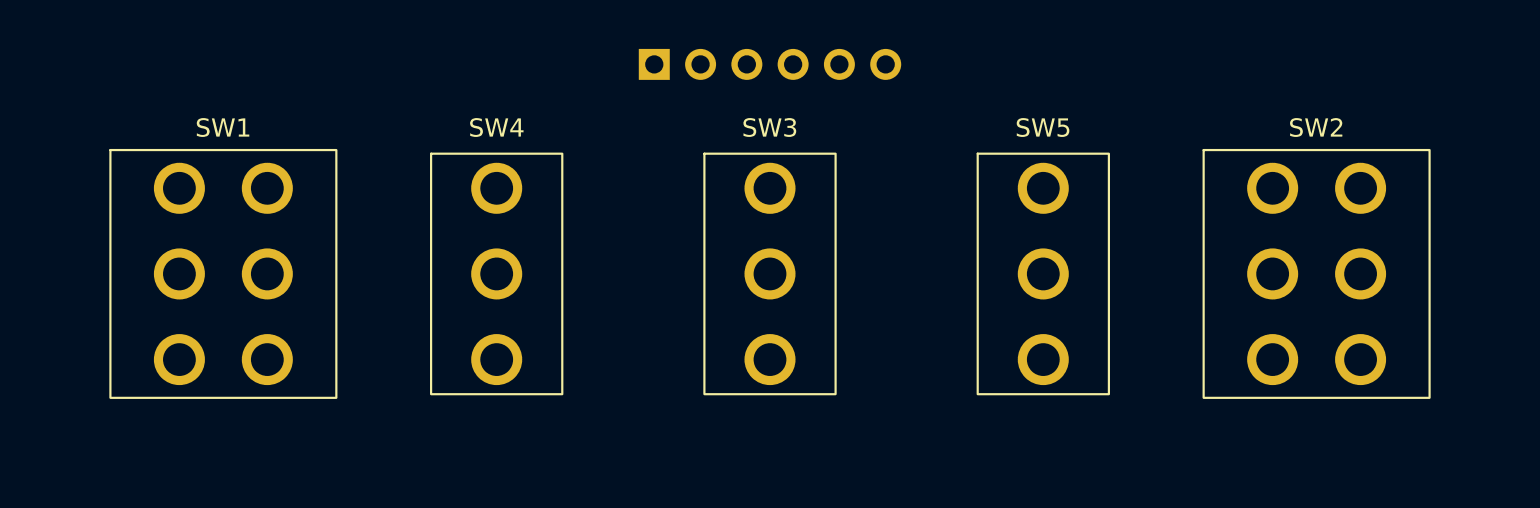
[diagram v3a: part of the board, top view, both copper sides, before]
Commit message: Addition of manual gate ongoing
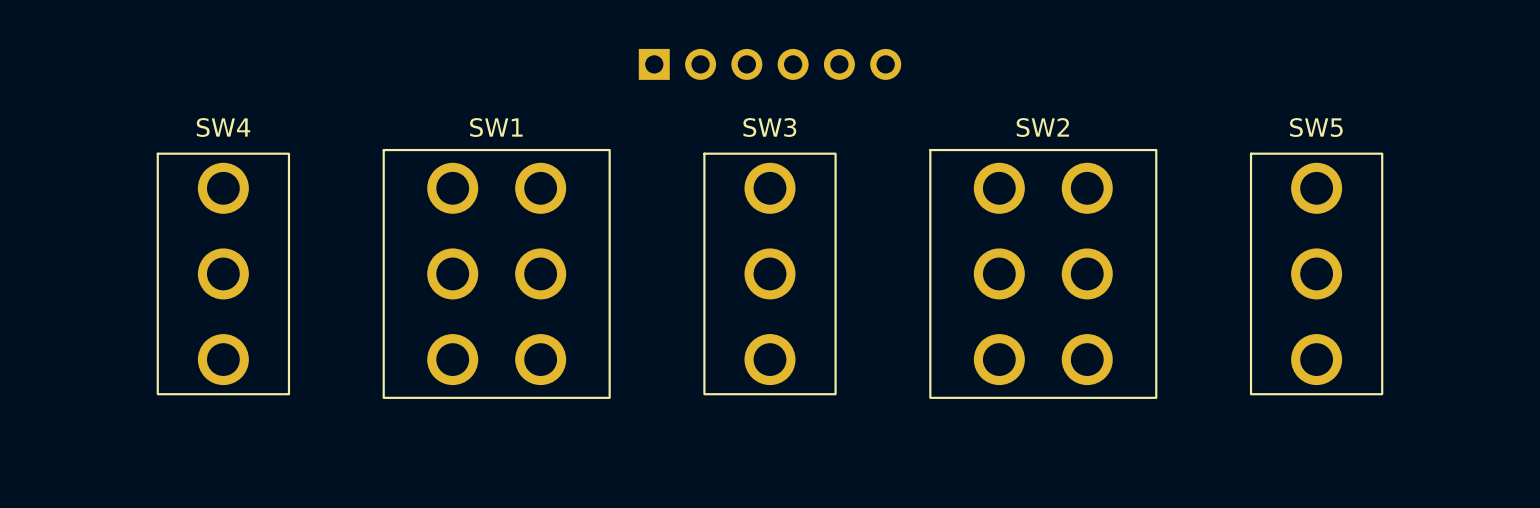
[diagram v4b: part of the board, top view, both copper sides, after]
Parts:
- moved SW1 15.0 mm to (85.0, 167.5)
- moved SW2 15.0 mm to (115.0, 167.5)
- moved SW4 15.0 mm to (70.0, 167.5)
- moved SW5 15.0 mm to (130.0, 167.5)
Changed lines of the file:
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@@
 	(footprint "SynthStuff:Toggle_Switch_2_Poles_TE"
 		(layer "F.Cu")
-		(at 70 167.5)
+		(at 85 167.5)
 		(property "Reference" "SW1"
 			(at 0 -8 0)
@@
 	(footprint "SynthStuff:Toggle_Switch_TE"
 		(layer "F.Cu")
-		(at 115 167.5)
+		(at 130 167.5)
 		(property "Reference" "SW5"
 			(at 0 -8 0)
@@
 	(footprint "SynthStuff:Toggle_Switch_TE"
 		(layer "F.Cu")
-		(at 85 167.5)
+		(at 70 167.5)
 		(property "Reference" "SW4"
 			(at 0 -8 0)
@@
 	(footprint "SynthStuff:Toggle_Switch_2_Poles_TE"
 		(layer "F.Cu")
-		(at 130 167.5)
+		(at 115 167.5)
 		(property "Reference" "SW2"
 			(at 0 -8 0)

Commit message: Added Output attenuation circuit
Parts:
- removed R132, R141, R143, R53, R62, R64: 100k, Resistor_THT:R_Axial_DIN0207_L6.3mm_D2.5mm_P7.62mm_Horizontal
- removed R144, R65: 1k, Resistor_THT:R_Axial_DIN0207_L6.3mm_D2.5mm_P7.62mm_Horizontal
- added C63: 100nF, Capacitor_THT:C_Disc_D4.3mm_W1.9mm_P5.00mm, F.Cu at (209.4, 222.0)
- added C64: 100nF, Capacitor_THT:C_Disc_D4.3mm_W1.9mm_P5.00mm, F.Cu at (224.0, 222.0)
- added R114: 1k, Resistor_THT:R_Axial_DIN0207_L6.3mm_D2.5mm_P7.62mm_Horizontal, F.Cu at (209.4, 208.2)
- added R159: 10k, Resistor_THT:R_Axial_DIN0207_L6.3mm_D2.5mm_P7.62mm_Horizontal, F.Cu at (209.4, 214.2)
- added R160: 47k, Resistor_THT:R_Axial_DIN0207_L6.3mm_D2.5mm_P7.62mm_Horizontal, F.Cu at (209.4, 218.2)
- added R161: 47k, Resistor_THT:R_Axial_DIN0207_L6.3mm_D2.5mm_P7.62mm_Horizontal, F.Cu at (224.0, 214.2)
- added R162: 10k, Resistor_THT:R_Axial_DIN0207_L6.3mm_D2.5mm_P7.62mm_Horizontal, F.Cu at (224.0, 218.2)
- added R35: 1k, Resistor_THT:R_Axial_DIN0207_L6.3mm_D2.5mm_P7.62mm_Horizontal, F.Cu at (224.0, 208.2)
- added RV45: 100k, Potentiometer_THT:Potentiometer_Bourns_3296X_Horizontal, F.Cu at (232.0, 190.2)
- added RV46: 100k, Potentiometer_THT:Potentiometer_Bourns_3296X_Horizontal, F.Cu at (232.0, 196.6)
- added RV47: 100k, Potentiometer_THT:Potentiometer_Bourns_3296X_Horizontal, F.Cu at (232.0, 202.9)
- added RV49: 100k, Potentiometer_THT:Potentiometer_Bourns_3296X_Horizontal, F.Cu at (217.4, 190.2)
- added RV50: 100k, Potentiometer_THT:Potentiometer_Bourns_3296X_Horizontal, F.Cu at (217.4, 196.6)
- added RV51: 100k, Potentiometer_THT:Potentiometer_Bourns_3296X_Horizontal, F.Cu at (217.4, 202.9)
- R135, R56: value 68K -> 100k
- RV10, RV14, RV34, RV4, RV40, RV44: value 100k -> C100k
- SW3: value SW_SPDT_321_OnOff -> SW_SPDT
- SW4, SW5: value SW_SPDT_321_OnOff -> SW_DPDT_x2_On-Off-(On); footprint SynthStuff:Toggle_Switch_TE -> SynthStuff:Toggle_Switch_2_Poles_TE
- U21: value TL072 -> TL074; footprint Package_DIP:DIP-8_W7.62mm_Socket -> Package_DIP:DIP-14_W7.62mm_Socket
- moved U21 7.86 mm to (96.2, 120.1)
- turned SW1 to 180 degrees
- turned SW2 to 180 degrees
- turned SW4 to 180 degrees
- turned SW5 to 180 degrees
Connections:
- J23 pad 2: GND -> Net-(J23B-Pin_2)
- J26 pad 2: GND -> Net-(J26B-Pin_2)
- J27 pad 3: GND -> Net-(J27C-Pin_3)
- J27 pad 4: GND -> Net-(J27D-Pin_4)
- J27 pad 5: Net-(J27E-Pin_5) -> /Core Circuit B/Out
- J27 pad 6: /Core Circuit B/Out -> Net-(J27F-Pin_6)
- R135 pad 1: Net-(R132-Pad2) -> Net-(U21A--)
- R145 pad 1: Net-(U21A-+) -> Net-(U21B-+)
- R146 pad 1: GND -> Net-(R146-Pad1)
- R146 pad 2: Net-(U21A-+) -> Net-(U21A--)
- R147 pad 1: Net-(U21B-+) -> Net-(U21C-+)
- R148 pad 1: GND -> Net-(U21D--)
- R148 pad 2: Net-(U21B-+) -> Net-(R114-Pad1)
- R56 pad 1: Net-(R53-Pad2) -> Net-(R56-Pad1)
- R56 pad 2: Net-(R56-Pad2) -> Net-(U21D--)
- R70 pad 1: Net-(R70-Pad1) -> Net-(R146-Pad1)
- R70 pad 2: Net-(J27A-Pin_1) -> Net-(J27C-Pin_3)
- R71 pad 1: Net-(U21A--) -> Net-(U21A-+)
- R71 pad 2: Net-(R70-Pad1) -> +12V
- R72 pad 2: Net-(U21A--) -> Net-(U21B--)
- R77 pad 1: Net-(R77-Pad1) -> Net-(R56-Pad1)
- R77 pad 2: Net-(J27E-Pin_5) -> Net-(J27D-Pin_4)
- R78 pad 1: Net-(U21B--) -> Net-(U21D-+)
- R78 pad 2: Net-(R77-Pad1) -> +12V
- R79 pad 2: Net-(U21B--) -> Net-(U21C--)
- SW4 pad 1: /Core Circuit A/Loop -> unconnected-(SW4A-A-Pad1)
- SW4 pad 3: unconnected-(SW4-A-Pad3) -> /Core Circuit A/Loop
- SW5 pad 1: /Core Circuit B/Loop -> unconnected-(SW5A-A-Pad1)
- SW5 pad 3: unconnected-(SW5-A-Pad3) -> /Core Circuit B/Loop
- U21 pad 1: Net-(R70-Pad1) -> Net-(R135-Pad2)
- U21 pad 4: -12V -> +12V
- U21 pad 7: Net-(R77-Pad1) -> Net-(R146-Pad1)
- U21 pad 8: +12V -> Net-(R56-Pad1)
